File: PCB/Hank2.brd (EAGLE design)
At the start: 256.5 x 129.5 mm, 100 parts, among them T1 2n2222, T2 2n2222, T3 2n2222, T4 2n2222, T5 2n2222, T6 2n2222, T7 2n2222, T8 2n2222, X3 Auto_Manual

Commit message: Changed v-regs and updated arduino program ready to test the ssrs
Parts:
- removed LF33CV, LF50ABV: (no value), v-reg:78XXL
- added IC1: LP2950CDT-3.3, v-reg:DPACK
- added IC2: LP2950CDT-5.0, v-reg:DPACK
- added NI1: 1k, rcl:0204/7
- added NI2: 2K, rcl:0204/7
- moved TX1 153.8 mm to (135.9, 33.0)
- moved TX2 151.0 mm to (135.9, 38.1)
- moved JUM_3.3V 98.9 mm to (8.50, 35.4)
- moved JUM_5.5V 98.9 mm to (8.50, 44.5)
- moved OLED_DISPLAY 88.0 mm to (82.0, 50.5)
- moved C_OLED 85.6 mm to (51.5, 54.1)
- moved RO22 79.4 mm to (123.2, 94.0)
- moved RO32 65.9 mm to (123.2, 87.6)
- moved RO52 61.0 mm to (124.5, 73.7)
- moved RO62 58.0 mm to (123.2, 68.6)
- moved RO42 56.9 mm to (121.9, 81.3)
- moved RO72 54.3 mm to (123.2, 64.8)
- moved RO82 50.6 mm to (124.5, 61.0)
- moved T8 31.8 mm to (97.8, 52.1)
- moved RO12 27.4 mm to (124.5, 99.1)
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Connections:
- new net N$32: ARDUINO.PB4, NI1.2
- new net NEW_IN: NI1.1, NI2.1, SV1.6
- net +3V3: now also IC1.3; no longer LF33CV.OUT
- net +5V: now also IC2.3; no longer LF50ABV.OUT
- net CP12: now also IC1.1, IC2.1; no longer LF33CV.IN, LF50ABV.IN
- net GND: now also IC1.4, IC2.4, NI2.2; no longer LF33CV.GND, LF50ABV.GND, SV1.6
- net N$12: now also T5.C; no longer T8.C
- net N$17: now also T6.C; no longer T7.C
- net N$18: now also T6.B; no longer T7.B
- net N$21: now also T7.C; no longer T6.C
- net N$22: now also T7.B; no longer T6.B
- net N$26: now also T8.C; no longer T5.C
- net N$34: now also T8.B; no longer T5.B
- net N$9: now also T5.B; no longer T8.B

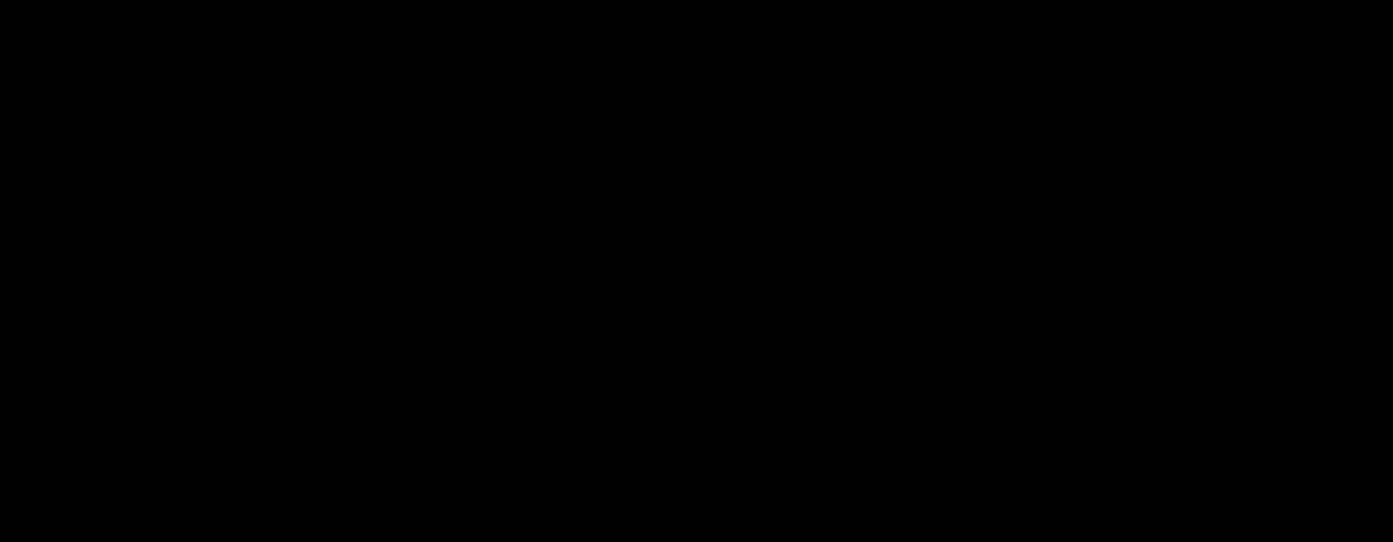
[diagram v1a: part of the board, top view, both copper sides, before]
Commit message: Tested the Atmega 328P and is fit for porpuse, Also got the Eagle library to add the Ic in the PCB
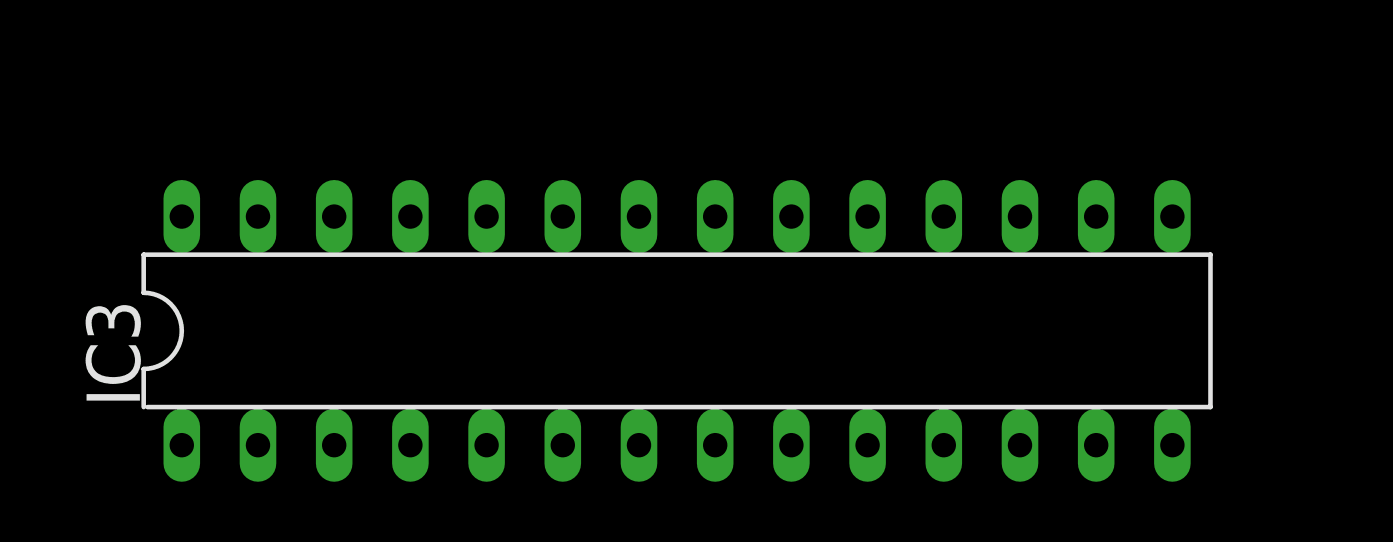
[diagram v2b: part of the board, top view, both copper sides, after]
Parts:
- added IC3: ATMEGA328-20P, atmega328:DIL28-3
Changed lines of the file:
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@@
 <layer number="54" name="bGND_GNDA" color="1" fill="9" visible="no" active="no"/>
 <layer number="56" name="wert" color="7" fill="1" visible="no" active="yes"/>
+<layer number="57" name="tCAD" color="7" fill="1" visible="no" active="no"/>
 <layer number="88" name="SimResults" color="9" fill="1" visible="yes" active="yes"/>
 <layer number="89" name="SimProbes" color="9" fill="1" visible="yes" active="yes"/>
@@
 <layer number="106" name="bPlate" color="7" fill="1" visible="no" active="yes"/>
 <layer number="107" name="Crop" color="7" fill="1" visible="no" active="yes"/>
+<layer number="108" name="fp8" color="7" fill="1" visible="no" active="yes"/>
+<layer number="109" name="fp9" color="7" fill="1" visible="no" active="yes"/>
+<layer number="110" name="fp0" color="7" fill="1" visible="no" active="yes"/>
+<layer number="111" name="LPC17xx" color="7" fill="1" visible="yes" active="yes"/>
+<layer number="112" name="tSilk" color="7" fill="1" visible="yes" active="yes"/>
 <layer number="116" name="Patch_BOT" color="9" fill="4" visible="no" active="yes"/>
 <layer number="121" name="_tsilk" color="7" fill="1" visible="yes" active="yes"/>
 <layer number="122" name="_bsilk" color="7" fill="1" visible="yes" active="yes"/>
+<layer number="123" name="tTestmark" color="7" fill="1" visible="no" active="yes"/>
+<layer number="124" name="bTestmark" color="7" fill="1" visible="no" active="yes"/>
+<layer number="125" name="_tNames" color="7" fill="1" visible="yes" active="yes"/>
+<layer number="126" name="_bNames" color="7" fill="1" visible="yes" active="yes"/>
+<layer number="127" name="_tValues" color="7" fill="1" visible="yes" active="yes"/>
+<layer number="128" name="_bValues" color="7" fill="1" visible="yes" active="yes"/>
+<layer number="131" name="tAdjust" color="7" fill="1" visible="no" active="yes"/>
+<layer number="132" name="bAdjust" color="7" fill="1" visible="no" active="yes"/>
 <layer number="144" name="Drill_legend" color="7" fill="1" visible="no" active="yes"/>
+<layer number="150" name="Notes" color="7" fill="1" visible="no" active="yes"/>
 <layer number="151" name="HeatSink" color="7" fill="1" visible="no" active="yes"/>
+<layer number="152" name="_bDocu" color="7" fill="1" visible="yes" active="yes"/>
+<layer number="153" name="FabDoc1" color="6" fill="1" visible="no" active="no"/>
+<layer number="154" name="FabDoc2" color="2" fill="1" visible="no" active="no"/>
+<layer number="155" name="FabDoc3" color="7" fill="15" visible="no" active="no"/>
+<layer number="199" name="Contour" color="7" fill="1" visible="yes" active="yes"/>
 <layer number="200" name="200bmp" color="1" fill="10" visible="yes" active="yes"/>
 <layer number="201" name="201bmp" color="2" fill="10" visible="yes" active="yes"/>
@@
 <layer number="215" name="215bmp" color="7" fill="1" visible="no" active="yes"/>
 <layer number="216" name="216bmp" color="7" fill="1" visible="no" active="yes"/>
+<layer number="217" name="217bmp" color="18" fill="1" visible="no" active="no"/>
+<layer number="218" name="218bmp" color="19" fill="1" visible="no" active="no"/>
+<layer number="219" name="219bmp" color="20" fill="1" visible="no" active="no"/>
+<layer number="220" name="220bmp" color="21" fill="1" visible="no" active="no"/>
+<layer number="221" name="221bmp" color="22" fill="1" visible="no" active="no"/>
+<layer number="222" name="222bmp" color="23" fill="1" visible="no" active="no"/>
+<layer number="223" name="223bmp" color="24" fill="1" visible="no" active="no"/>
+<layer number="224" name="224bmp" color="25" fill="1" visible="no" active="no"/>
+<layer number="248" name="Housing" color="7" fill="1" visible="yes" active="yes"/>
+<layer number="249" name="Edge" color="7" fill="1" visible="yes" active="yes"/>
 <layer number="250" name="Descript" color="3" fill="1" visible="no" active="no"/>
 <layer number="251" name="SMDround" color="12" fill="11" visible="no" active="no"/>
@@
 <element name="IC1" library="v-reg" package="DPACK" value="LP2950CDT-3.3" x="57.15" y="36.83"/>
 <element name="IC2" library="v-reg" package="DPACK" value="LP2950CDT-5.0" x="43.18" y="38.1"/>
+<element name="IC3" library="atmega328" package="DIL28-3" value="ATMEGA328-20P" x="6.35" y="-16.51"/>
 </elements>
 <signals>

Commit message: Added Atmega 328-20P to the pcb and wired, still to be verified and tidied up
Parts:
- removed ARDUINO: ARDUINO_MICRO, HankLibraries:ARDUINOMICRO_FOOTPRINT
- added C_RTC1, C_USD1, C_USD2, C_USD3: 0.1uF, rcl:C025-024X044
- added D1: 1N4148DO35-7, diode:DO35-7
- added FTDI: (no value), con-lstb:MA06-1
- added Q1: 16M, crystal:HC49/S
- added RDX: 10k, rcl:0204/7
- added RI9: 330, rcl:0204/7
- added S1: DTE6, switch-misc:DTE6
- added SV4: (no value), con-lstb:MA03-2
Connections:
- removed net ARD_RX: ARDUINO.RX
- removed net ARD_TX: TX1.1, TX2.2
- new net N$35: C_USD2.1, IC3.10, Q1.1
- new net N$39: IC3.16, NI1.2
- new net RTS: C_RTC1.1, FTDI.6
- new net RXD: RDX.2
- new net TXD: FTDI.4
- new net U_RESET: C_RTC1.2, D1.A, IC3.1, RI9.2, S1.1, S1.2, SV4.5
- new net U_RX: IC3.2, SV1.7
- new net U_TX: IC3.3, TX1.2
- new net U_TX_3: SV1.8, TX1.1, TX2.2
- net +5V: now also C_USD3.2, D1.C, FTDI.3, IC3.20, IC3.21, IC3.7, RI9.1, SV4.2; no longer ARDUINO.VIN
- net AUTO_MANUAL: now also IC3.17, SV4.4; no longer ARDUINO.PB2
- net GND: now also C_USD1.2, C_USD2.2, C_USD3.1, FTDI.1, FTDI.2, IC3.22, IC3.8, S1.3, S1.4, SV4.6, T4.E, T8.E; no longer ARDUINO.GND, ARDUINO.GND2
- net IN1: now also IC3.23; no longer ARDUINO.PF7
- net IN2: now also IC3.24; no longer ARDUINO.PF6
- net IN3: now also IC3.25; no longer ARDUINO.PF5
- net IN4: now also IC3.26; no longer ARDUINO.PF4
- net IN5: now also IC3.27; no longer ARDUINO.PF1
- net IN6: now also IC3.28; no longer ARDUINO.PF0
- net IN7: now also IC3.18, SV4.1; no longer ARDUINO.PB3
- net IN8: now also IC3.19, SV4.3; no longer ARDUINO.PB1
- net N$32: now also C_USD1.1, IC3.9, Q1.2; no longer ARDUINO.PB4, NI1.2
- net N$6: now also FTDI.5, RDX.1; no longer ARDUINO.TX, TX1.2
- net OUT1: now also IC3.4; no longer ARDUINO.PC7
- net OUT2: now also IC3.5; no longer ARDUINO.PD6
- net OUT3: now also IC3.6; no longer ARDUINO.PB7
- net OUT4: now also IC3.11; no longer ARDUINO.PB6
- net OUT5: now also IC3.12; no longer ARDUINO.PB5
- net OUT6: now also IC3.13; no longer ARDUINO.PD7
- net OUT7: now also IC3.14; no longer ARDUINO.PC6
- net OUT8: now also IC3.15; no longer ARDUINO.PD0
- net SERIAL_RXD: no longer SV1.7
- net SERIAL_TXD: no longer SV1.8

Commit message: Started arranging components in the PCB
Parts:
- removed 3.3V, 5V: (no value), led:LED3MM
- removed C_RTC1, C_USD1, C_USD2, C_USD3: 0.1uF, rcl:C025-024X044
- removed D1: 1N4148DO35-7, diode:DO35-7
- removed IC1: LP2950CDT-3.3, v-reg:DPACK
- removed IC2: LP2950CDT-5.0, v-reg:DPACK
- removed JUM_3.3V, JUM_5.5V: 22-23-2021, con-molex:22-23-2021
- removed MOUT: (no value), con-ptr500:AK300/10
- removed NI1, TX1: 1k, rcl:0204/7
- removed NI2, TX2: 2K, rcl:0204/7
- removed Q1: 16M, crystal:HC49/S
- removed R2: (no value), rcl:0204/7
- removed RI9: 330, rcl:0204/7
- removed S1: DTE6, switch-misc:DTE6
- removed X3: Auto_Manual, con-molex:22-23-2021
- added AUTO: Auto_Manual, con-molex:22-23-2021
- added C_U, C_URTS, C_UXTAL1, C_UXTAL2: 0.1uF, rcl:C025-024X044
- added D_3V3, D_5V: (no value), led:LED3MM
- added D_URES: 1N4148DO35-7, diode:DO35-7
- added J_3.3V, J_5.5V: Jumper, con-molex:22-23-2021
- added REG_3V3: LP2950CDT-3.3, v-reg:DPACK
- added REG_5V: LP2950CDT-5.0, v-reg:DPACK
- added R_AUTO: (no value), rcl:0204/7
- added R_NI1, R_UTX1: 1k, rcl:0204/7
- added R_NI2, R_UTX2: 2K, rcl:0204/7
- added R_URES: 330, rcl:0204/7
- added URES: DTE6, switch-misc:DTE6
- added X1, X2: (no value), con-ptr500:AK300/5
- added XTALU: 16M, crystal:HC49/S
- moved RDX 264.8 mm to (105.4, 47.0)
- moved SV4 247.3 mm to (130.8, 27.9)
- moved SV2 216.8 mm to (5.08, 108.0), turned to 270 degrees
- moved SV1 199.4 mm to (9.14, 107.7)
- moved FTDI 186.7 mm to (110.5, 61.0), turned to 270 degrees
- moved IC3 157.4 mm to (148.6, 50.8), turned to 270 degrees
- moved RI8 90.9 mm to (176.0, 72.0)
- moved RI7 84.4 mm to (176.0, 67.7)
- moved RI6 78.4 mm to (176.0, 63.4)
- moved RI5 73.7 mm to (176.0, 60.4)
- moved IN_BUTTONS 70.8 mm to (163.8, 62.2), turned to 90 degrees
- moved RI4 69.5 mm to (176.0, 57.3)
- moved RI3 65.9 mm to (176.0, 54.3)
- moved RI2 63.1 mm to (176.0, 51.2)
- moved RI1 61.0 mm to (176.0, 48.2)
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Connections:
- removed net N$14: SV1.10
- net +3V3: now also AUTO.1, D_3V3.A, J_5.5V.1, REG_3V3.3; no longer 3.3V.A, IC1.3, JUM_5.5V.1, X3.1
- net +5V: now also C_U.2, D_5V.A, D_URES.C, J_3.3V.1, REG_5V.3, R_URES.1; no longer 5V.A, C_USD3.2, D1.C, IC2.3, JUM_3.3V.1, RI9.1
- net AUTO_MANUAL: now also AUTO.2, R_AUTO.2; no longer R2.2, X3.2
- net CP12: now also REG_3V3.1, REG_5V.1; no longer IC1.1, IC2.1
- net GND: now also C_U.1, C_UXTAL1.2, C_UXTAL2.2, REG_3V3.4, REG_5V.4, R_AUTO.1, R_NI2.2, R_UTX2.1, T1.E, T2.E, T5.E, T6.E, T7.E, URES.3, URES.4; no longer C_USD1.2, C_USD2.2, C_USD3.1, IC1.4, IC2.4, NI2.2, R2.1, S1.3, S1.4, TX2.1
- net L1-1: now also X1.5; no longer MOUT.1
- net L1-2: now also X2.5; no longer MOUT.6
- net MO1: now also X1.1; no longer MOUT.2
- net MO2: now also X1.2; no longer MOUT.3
- net MO3: now also X1.3; no longer MOUT.4
- net MO4: now also X1.4; no longer MOUT.5
- net MO5: now also X2.1; no longer MOUT.7
- net MO6: now also X2.2; no longer MOUT.8
- net MO7: now also X2.3; no longer MOUT.9
- net MO8: now also X2.4; no longer MOUT.10
- net N$1: now also J_3.3V.2; no longer JUM_3.3V.2
- net N$2: now also J_5.5V.2; no longer JUM_5.5V.2
- net N$32: now also C_UXTAL1.1, XTALU.2; no longer C_USD1.1, Q1.2
- net N$35: now also C_UXTAL2.1, XTALU.1; no longer C_USD2.1, Q1.1
- net N$39: now also R_NI1.2; no longer NI1.2
- net N$4: now also D_5V.K; no longer 5V.K
- net N$5: now also D_3V3.K; no longer 3.3V.K
- net NEW_IN: now also R_NI1.1, R_NI2.1; no longer NI1.1, NI2.1
- net RTS: now also C_URTS.1; no longer C_RTC1.1
- net SCL: now also SV1.10
- net SDA: now also SV1.9
- net U_RESET: now also C_URTS.2, D_URES.A, R_URES.2, URES.1, URES.2; no longer C_RTC1.2, D1.A, RI9.2, S1.1, S1.2
- net U_TX: now also R_UTX1.2; no longer TX1.2
- net U_TX_3: now also R_UTX1.1, R_UTX2.2; no longer TX1.1, TX2.2

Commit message: Added parts schedule
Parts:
- IN_BUTTONS: value (none) -> User Inputs
- RI8, R_AUTO: value (none) -> 330
- RO33: value (none) -> 1k
- X1: value (none) -> Sockets 1
- X2: value (none) -> Sockets 2
- moved RDX 35.9 mm to (135.9, 66.0)
- moved RI8 22.7 mm to (172.7, 49.5)
- moved RI1 19.4 mm to (172.7, 67.3)
- moved C_U 17.7 mm to (137.2, 50.8), turned to 90 degrees
- moved RI7 16.0 mm to (172.7, 52.1)
- moved C_URTS 14.2 mm to (110.5, 67.3)
- moved RI2 13.9 mm to (172.7, 64.8)
- moved AUTO 11.4 mm to (7.62, 59.7)
- moved R_AUTO 10.2 mm to (17.8, 61.0), turned to 180 degrees
- moved RI6 9.39 mm to (172.7, 54.6)
- moved XTALU 8.98 mm to (129.5, 47.0)
- moved RI3 8.61 mm to (172.7, 62.2)
- moved J_3.3V 8.50 mm to (7.62, 47.0)
- moved J_5.5V 8.50 mm to (7.62, 53.3)
- moved C_UXTAL1 7.73 mm to (123.2, 49.5)
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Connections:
- removed net N$10: U$4.KEY
- removed net N$13: U$4.5V
- removed net N$15: R51.2, RO52.2
- removed net N$19: R61.2, RO62.2
- removed net N$24: RO71.2, RO72.2
- removed net N$28: RO81.2, RO82.2
- removed net N$36: RO21.2, RO22.2
- removed net N$40: RO31.2, RO32.2
- removed net N$44: RO41.2, RO42.2
- removed net N$7: RI1.2, RI2.2, RI3.2, RI4.2, RI5.2, RI6.2, RI7.2, RI8.2
- removed net RXD: RDX.2
- removed net SERIAL_RXD: U$4.RXD
- removed net SERIAL_TXD: U$4.TXD
- removed net TXD: FTDI.4
- new net BT_RX: SV1.4, U$4.RXD
- new net BT_TX: SV1.5, U$4.TXD
- net GND: now also RI1.2, RI2.2, RI3.2, RI4.2, RI5.2, RI6.2, RI7.2, RI8.2; no longer SV1.4, SV1.5
- net IN1: now also IC3.18, IN_BUTTONS.9, RI8.1; no longer IC3.23, IN_BUTTONS.2, RI1.1
- net IN2: now also IC3.19, IN_BUTTONS.8, RI7.1; no longer IC3.24, IN_BUTTONS.3, RI2.1
- net IN3: now also IC3.23, IN_BUTTONS.7, RI6.1; no longer IC3.25, IN_BUTTONS.4, RI3.1
- net IN4: now also IC3.24, IN_BUTTONS.6, RI5.1; no longer IC3.26, IN_BUTTONS.5, RI4.1
- net IN5: now also IC3.25, IN_BUTTONS.5, RI4.1; no longer IC3.27, IN_BUTTONS.6, RI5.1
- net IN6: now also IC3.26, IN_BUTTONS.4, RI3.1; no longer IC3.28, IN_BUTTONS.7, RI6.1
- net IN7: now also IC3.27, IN_BUTTONS.3, RI2.1; no longer IC3.18, IN_BUTTONS.8, RI7.1
- net IN8: now also IC3.28, IN_BUTTONS.2, RI1.1; no longer IC3.19, IN_BUTTONS.9, RI8.1
- net OUT2: now also RO21.2, RO22.2
- net OUT3: now also RO31.2, RO32.2
- net OUT4: now also RO41.2, RO42.2
- net OUT5: now also R51.2, RO52.2
- net OUT6: now also R61.2, RO62.2
- net OUT7: now also RO71.2, RO72.2
- net OUT8: now also RO81.2, RO82.2
- net U_RX: now also FTDI.4
- net U_TX: now also RDX.2

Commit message: Updating parts footprint in the brd
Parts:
- removed CP02, CP32, CP52: 100n, rcl:E5-8,5
- added D_PSU: 1N4148DO35-7, diode:DO35-7
- CP31, CP51: value 100u -> 22uF
- moved CP31 20.1 mm to (55.9, 21.6)
- moved PR_3.3V 17.8 mm to (71.1, 24.1)
- moved PR_5V 16.5 mm to (71.1, 7.62)
- moved U$7 12.8 mm to (83.8, 91.4)
- moved CP51 12.5 mm to (55.9, 11.4)
- moved REG_3V3 12.0 mm to (44.5, 29.2)
- moved D_5V 11.4 mm to (71.1, 16.5), turned to 270 degrees
- moved D_3V3 11.4 mm to (71.1, 33.0), turned to 270 degrees
- moved REG_5V 10.2 mm to (45.7, 12.7)
- moved CP01 9.16 mm to (33.0, 16.5), turned to 270 degrees
- moved PSU 7.62 mm to (7.62, 16.5), turned to 270 degrees
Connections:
- new net N$7: D_PSU.A, PSU.1
- net +3V3: no longer CP32.+
- net +5V: no longer CP52.+
- net CP12: now also D_PSU.C; no longer CP02.+, PSU.1
- net GND: no longer CP02.-, CP32.-, CP52.-
